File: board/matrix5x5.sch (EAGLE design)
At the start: 26 parts

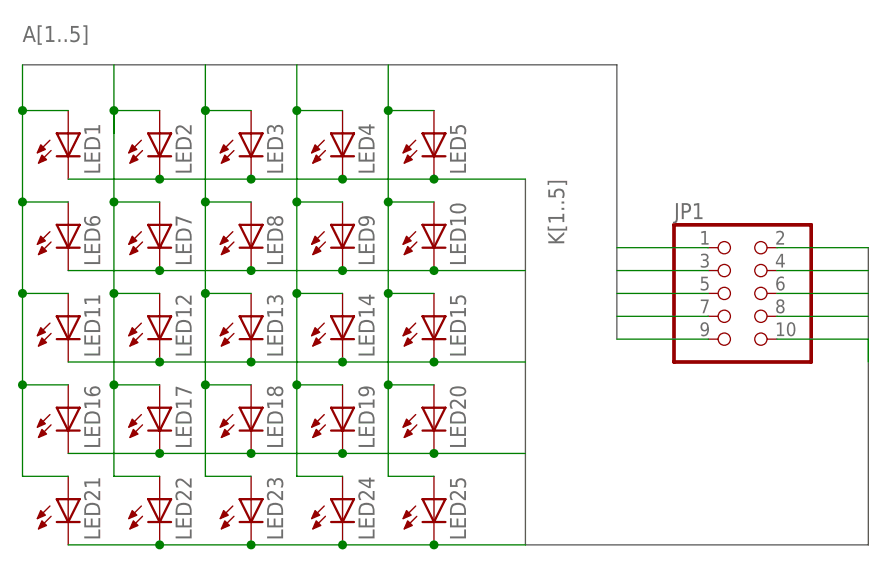
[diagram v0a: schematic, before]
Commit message: board: fix net name and add artwork
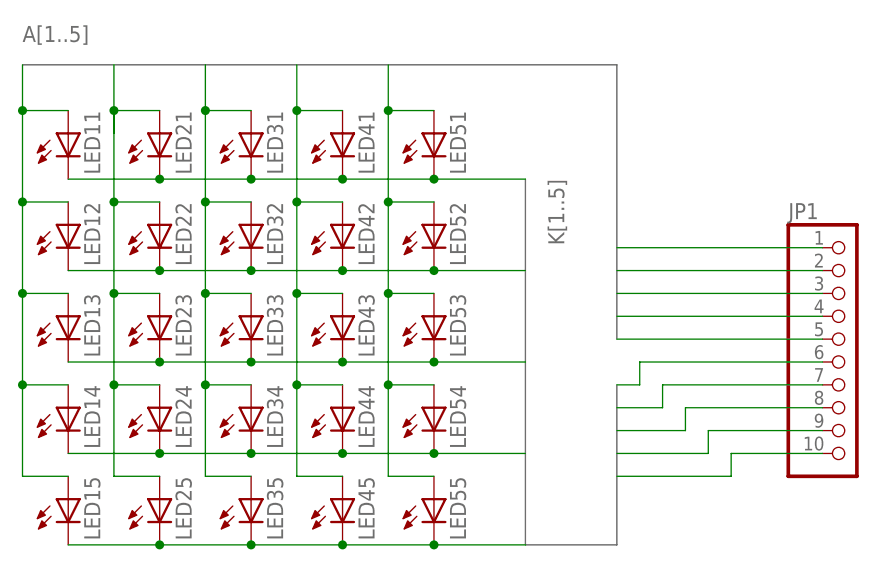
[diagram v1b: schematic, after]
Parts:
- removed LED1, LED10, LED16, LED17, LED18, LED19, LED2, LED20, LED3, LED4, LED5, LED6, LED7, LED8, LED9: (no value), led:LEDCHIPLED_0805
- added LED31, LED32, LED33, LED34, LED35, LED41, LED42, LED43, LED44, LED45, LED51, LED52, LED53, LED54, LED55: (no value), led:LED5MM
- JP1: device pinhead:PINHD-2X5 -> pinhead:PINHD-1X10
- LED11, LED12, LED13, LED14, LED15, LED21, LED22, LED23, LED24, LED25: device led:LEDCHIPLED_0805 -> led:LED5MM
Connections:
- net A1: now also LED12.A, LED13.A, LED14.A, LED15.A; no longer LED1.A, LED16.A, LED21.A, LED6.A
- net A2: now also JP1.2, LED21.A, LED23.A, LED24.A, LED25.A; no longer JP1.3, LED12.A, LED17.A, LED2.A, LED7.A
- net A3: now also JP1.3, LED31.A, LED32.A, LED33.A, LED34.A, LED35.A; no longer JP1.5, LED13.A, LED18.A, LED23.A, LED3.A, LED8.A
- net A4: now also JP1.4, LED41.A, LED42.A, LED43.A, LED44.A, LED45.A; no longer JP1.7, LED14.A, LED19.A, LED24.A, LED4.A, LED9.A
- net A5: now also JP1.5, LED51.A, LED52.A, LED53.A, LED54.A, LED55.A; no longer JP1.9, LED10.A, LED15.A, LED20.A, LED25.A, LED5.A
- net K1: now also JP1.6, LED11.C, LED21.C, LED31.C, LED41.C, LED51.C; no longer JP1.2, LED1.C, LED2.C, LED3.C, LED4.C, LED5.C
- net K2: now also JP1.7, LED12.C, LED22.C, LED32.C, LED42.C, LED52.C; no longer JP1.4, LED10.C, LED6.C, LED7.C, LED8.C, LED9.C
- net K3: now also JP1.8, LED23.C, LED33.C, LED43.C, LED53.C; no longer JP1.6, LED11.C, LED12.C, LED14.C, LED15.C
- net K4: now also JP1.9, LED14.C, LED24.C, LED34.C, LED44.C, LED54.C; no longer JP1.8, LED16.C, LED17.C, LED18.C, LED19.C, LED20.C
- net K5: now also LED15.C, LED35.C, LED45.C, LED55.C; no longer LED21.C, LED22.C, LED23.C, LED24.C
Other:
- moved on the sheet: JP1, LED11, LED12, LED13, LED14, LED15, LED21, LED22, LED23, LED24, LED25
